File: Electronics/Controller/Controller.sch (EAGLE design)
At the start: 20 parts, among them Q1 IRFD9014, U1 GY-521MPU6050, X1 Battery, X2 Switch

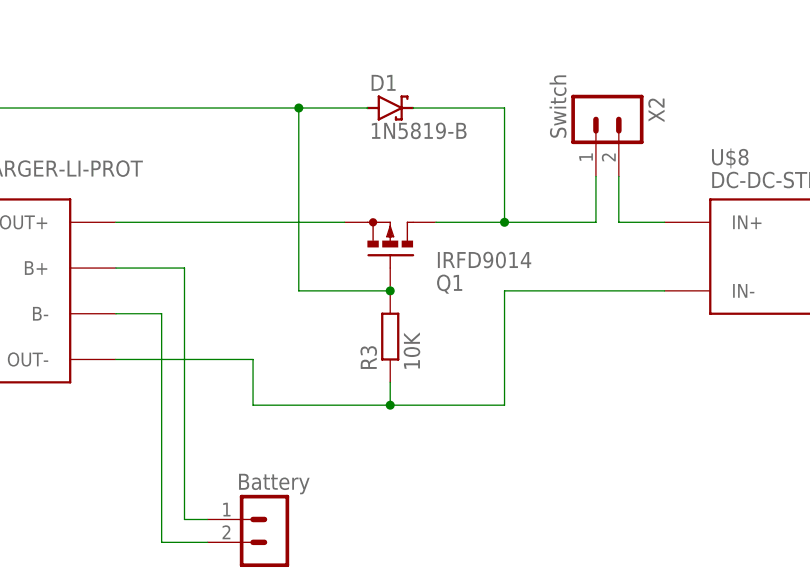
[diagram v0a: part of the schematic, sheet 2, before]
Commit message: Completed all routes
Completed all routes and changed the P-Channel mosfet to a NDP6020P
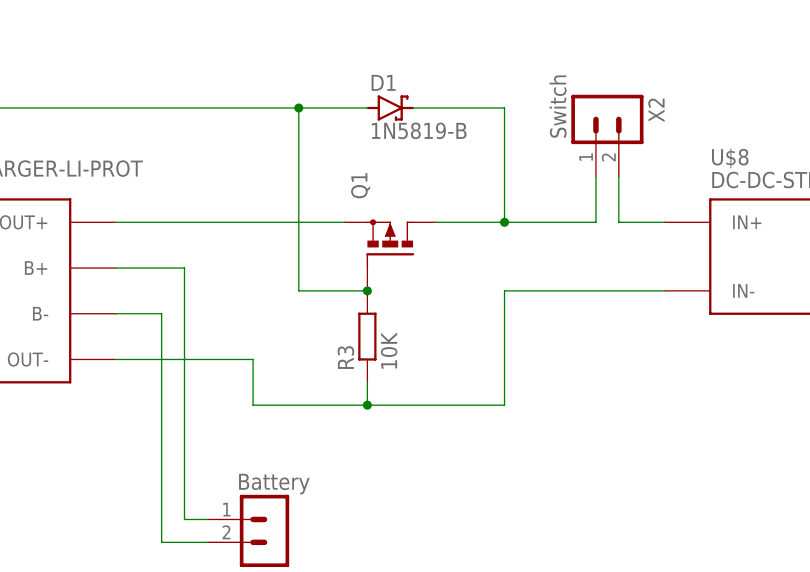
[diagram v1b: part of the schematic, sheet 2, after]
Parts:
- Q1: value IRFD9014 -> (none); device transistor-small-signal:IRFD9120 -> transistor-power:PMOSFET_PTO220BH
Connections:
- new net SW2: R1.2, RIGHT_STICK.SEL-, U$1.12/MISO
- net SW1: no longer R1.2, RIGHT_STICK.SEL-, U$1.12/MISO
- net X-AXIS1: now also U$1.15/A1/T; no longer U$1.14/A0
- net Y-AXIS1: now also U$1.14/A0; no longer U$1.15/A1/T
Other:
- moved on the sheet: R3
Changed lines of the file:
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@@
 <part name="P+4" library="supply1" library_urn="urn:adsk.eagle:library:371" deviceset="+5V" device="" value="+5V_Source"/>
 <part name="GND5" library="supply1" library_urn="urn:adsk.eagle:library:371" deviceset="GND" device="" value="GND_Source"/>
-<part name="Q1" library="transistor-small-signal" library_urn="urn:adsk.eagle:library:401" deviceset="IRFD9120" device="" package3d_urn="urn:adsk.eagle:package:29750/1" value="IRFD9014"/>
 <part name="R3" library="rcl" library_urn="urn:adsk.eagle:library:334" deviceset="R-EU_" device="0207/10" package3d_urn="urn:adsk.eagle:package:23491/2" value="10K"/>
 <part name="D1" library="diode" library_urn="urn:adsk.eagle:library:210" deviceset="1N581*" device="" package3d_urn="urn:adsk.eagle:package:43421/1" technology="9-B"/>
@@
 <part name="P+5" library="supply1" library_urn="urn:adsk.eagle:library:371" deviceset="+5V" device=""/>
 <part name="GND8" library="supply1" library_urn="urn:adsk.eagle:library:371" deviceset="GND" device=""/>
+<part name="Q1" library="transistor-power" library_urn="urn:adsk.eagle:library:400" deviceset="PMOSFET_P" device="TO220BH" package3d_urn="urn:adsk.eagle:package:29490/1"/>
 </parts>
 <sheets>
@@
 </segment>
 <segment>
+<wire x1="43.18" y1="180.34" x2="35.56" y2="180.34" width="0.1524" layer="91"/>
+<label x="35.56" y="180.34" size="1.016" layer="95" rot="R180" xref="yes"/>
+<pinref part="U$1" gate="G$1" pin="15/A1/T"/>
+</segment>
+</net>
+<net name="Y-AXIS1" class="0">
+<segment>
+<pinref part="LEFT_STICK" gate="G$1" pin="H"/>
+<wire x1="335.28" y1="220.98" x2="314.96" y2="220.98" width="0.1524" layer="91"/>
+<label x="314.96" y="220.98" size="1.016" layer="95" rot="R180" xref="yes"/>
+</segment>
+<segment>
 <wire x1="43.18" y1="182.88" x2="35.56" y2="182.88" width="0.1524" layer="91"/>
 <label x="35.56" y="182.88" size="1.016" layer="95" rot="R180" xref="yes"/>
 <pinref part="U$1" gate="G$1" pin="14/A0"/>
-</segment>
-</net>
-<net name="Y-AXIS1" class="0">
-<segment>
-<pinref part="LEFT_STICK" gate="G$1" pin="H"/>
-<wire x1="335.28" y1="220.98" x2="314.96" y2="220.98" width="0.1524" layer="91"/>
-<label x="314.96" y="220.98" size="1.016" layer="95" rot="R180" xref="yes"/>
-</segment>
-<segment>
-<wire x1="43.18" y1="180.34" x2="35.56" y2="180.34" width="0.1524" layer="91"/>
-<label x="35.56" y="180.34" size="1.016" layer="95" rot="R180" xref="yes"/>
-<pinref part="U$1" gate="G$1" pin="15/A1/T"/>
 </segment>
 </net>
@@
 </segment>
 <segment>
-<label x="314.96" y="172.72" size="1.016" layer="95" rot="R180" xref="yes"/>
-<pinref part="RIGHT_STICK" gate="G$1" pin="SEL-"/>
-<pinref part="R1" gate="G$1" pin="2"/>
-<wire x1="335.28" y1="172.72" x2="330.2" y2="172.72" width="0.1524" layer="91"/>
-<wire x1="330.2" y1="172.72" x2="314.96" y2="172.72" width="0.1524" layer="91"/>
-<junction x="330.2" y="172.72"/>
-</segment>
-<segment>
 <label x="35.56" y="190.5" size="1.016" layer="95" rot="R180" xref="yes"/>
 <wire x1="43.18" y1="190.5" x2="35.56" y2="190.5" width="0.1524" layer="91"/>
 <pinref part="U$1" gate="G$1" pin="11/MOSI"/>
-</segment>
-<segment>
-<label x="35.56" y="187.96" size="1.016" layer="95" rot="R180" xref="yes"/>
-<wire x1="43.18" y1="187.96" x2="35.56" y2="187.96" width="0.1524" layer="91"/>
-<pinref part="U$1" gate="G$1" pin="12/MISO"/>
 </segment>
 </net>
@@
 </segment>
 </net>
+<net name="SW2" class="0">
+<segment>
+<label x="35.56" y="187.96" size="1.016" layer="95" rot="R180" xref="yes"/>
+<wire x1="43.18" y1="187.96" x2="35.56" y2="187.96" width="0.1524" layer="91"/>
+<pinref part="U$1" gate="G$1" pin="12/MISO"/>
+</segment>
+<segment>
+<label x="314.96" y="172.72" size="1.016" layer="95" rot="R180" xref="yes"/>
+<pinref part="RIGHT_STICK" gate="G$1" pin="SEL-"/>
+<pinref part="R1" gate="G$1" pin="2"/>
+<wire x1="335.28" y1="172.72" x2="330.2" y2="172.72" width="0.1524" layer="91"/>
+<wire x1="330.2" y1="172.72" x2="314.96" y2="172.72" width="0.1524" layer="91"/>
+<junction x="330.2" y="172.72"/>
+</segment>
+</net>
 </nets>
 </sheet>
@@
 <attribute name="VALUE" x="48.26" y="86.36" size="1.778" layer="96"/>
 </instance>
-<instance part="Q1" gate="A" x="116.84" y="106.68" smashed="yes" rot="R90">
-<attribute name="NAME" x="121.92" y="101.6" size="1.778" layer="95"/>
-<attribute name="VALUE" x="121.92" y="104.14" size="1.778" layer="96"/>
-</instance>
-<instance part="R3" gate="G$1" x="116.84" y="96.52" smashed="yes" rot="R90">
-<attribute name="NAME" x="115.3414" y="92.71" size="1.778" layer="95" rot="R90"/>
-<attribute name="VALUE" x="120.142" y="92.71" size="1.778" layer="96" rot="R90"/>
+<instance part="R3" gate="G$1" x="114.3" y="96.52" smashed="yes" rot="R90">
+<attribute name="NAME" x="112.8014" y="92.71" size="1.778" layer="95" rot="R90"/>
+<attribute name="VALUE" x="117.602" y="92.71" size="1.778" layer="96" rot="R90"/>
 </instance>
 <instance part="D1" gate="G$1" x="116.84" y="121.92" smashed="yes">
@@
 <attribute name="VALUE" x="134.62" y="125.73" size="1.778" layer="96" rot="R270"/>
 <attribute name="NAME" x="145.542" y="123.19" size="1.778" layer="95" rot="R270"/>
+</instance>
+<instance part="Q1" gate="G$1" x="116.84" y="106.68" smashed="yes" rot="R90">
+<attribute name="NAME" x="114.3" y="111.76" size="1.778" layer="95" rot="R90"/>
+<attribute name="VALUE" x="116.84" y="111.76" size="1.778" layer="96" rot="R90"/>
 </instance>
 </instances>
@@
 <pinref part="U$5" gate="G$1" pin="OUT+"/>
 <wire x1="86.36" y1="109.22" x2="111.76" y2="109.22" width="0.1524" layer="91"/>
-<pinref part="Q1" gate="A" pin="S"/>
+<pinref part="Q1" gate="G$1" pin="S"/>
 </segment>
 </net>
@@
 <wire x1="50.8" y1="121.92" x2="50.8" y2="124.46" width="0.1524" layer="91"/>
 <junction x="50.8" y="121.92"/>
-<pinref part="Q1" gate="A" pin="G"/>
 <pinref part="R3" gate="G$1" pin="2"/>
-<wire x1="116.84" y1="101.6" x2="106.68" y2="101.6" width="0.1524" layer="91"/>
-<junction x="116.84" y="101.6"/>
+<wire x1="114.3" y1="101.6" x2="106.68" y2="101.6" width="0.1524" layer="91"/>
 <wire x1="106.68" y1="101.6" x2="106.68" y2="121.92" width="0.1524" layer="91"/>
 <junction x="106.68" y="121.92"/>
+<pinref part="Q1" gate="G$1" pin="G"/>
+<junction x="114.3" y="101.6"/>
 </segment>
 <segment>
@@
 <segment>
 <pinref part="R3" gate="G$1" pin="1"/>
-<wire x1="116.84" y1="88.9" x2="116.84" y2="91.44" width="0.1524" layer="91"/>
-<wire x1="101.6" y1="88.9" x2="116.84" y2="88.9" width="0.1524" layer="91"/>
+<wire x1="114.3" y1="88.9" x2="114.3" y2="91.44" width="0.1524" layer="91"/>
+<wire x1="101.6" y1="88.9" x2="114.3" y2="88.9" width="0.1524" layer="91"/>
 <pinref part="U$5" gate="G$1" pin="OUT-"/>
 <wire x1="86.36" y1="93.98" x2="101.6" y2="93.98" width="0.1524" layer="91"/>
@@
 <pinref part="U$8" gate="G$1" pin="IN-"/>
 <wire x1="147.32" y1="101.6" x2="129.54" y2="101.6" width="0.1524" layer="91"/>
-<wire x1="116.84" y1="88.9" x2="129.54" y2="88.9" width="0.1524" layer="91"/>
-<junction x="116.84" y="88.9"/>
+<wire x1="114.3" y1="88.9" x2="129.54" y2="88.9" width="0.1524" layer="91"/>
+<junction x="114.3" y="88.9"/>
 </segment>
 </net>
 <net name="N$4" class="0">
 <segment>
-<pinref part="Q1" gate="A" pin="D"/>
 <wire x1="121.92" y1="109.22" x2="129.54" y2="109.22" width="0.1524" layer="91"/>
 <pinref part="D1" gate="G$1" pin="C"/>
@@
 <wire x1="139.7" y1="109.22" x2="139.7" y2="114.3" width="0.1524" layer="91"/>
 <junction x="129.54" y="109.22"/>
-</segment>
-</net>
+<pinref part="Q1" gate="G$1" pin="D"/>
+</segment>
+</net>

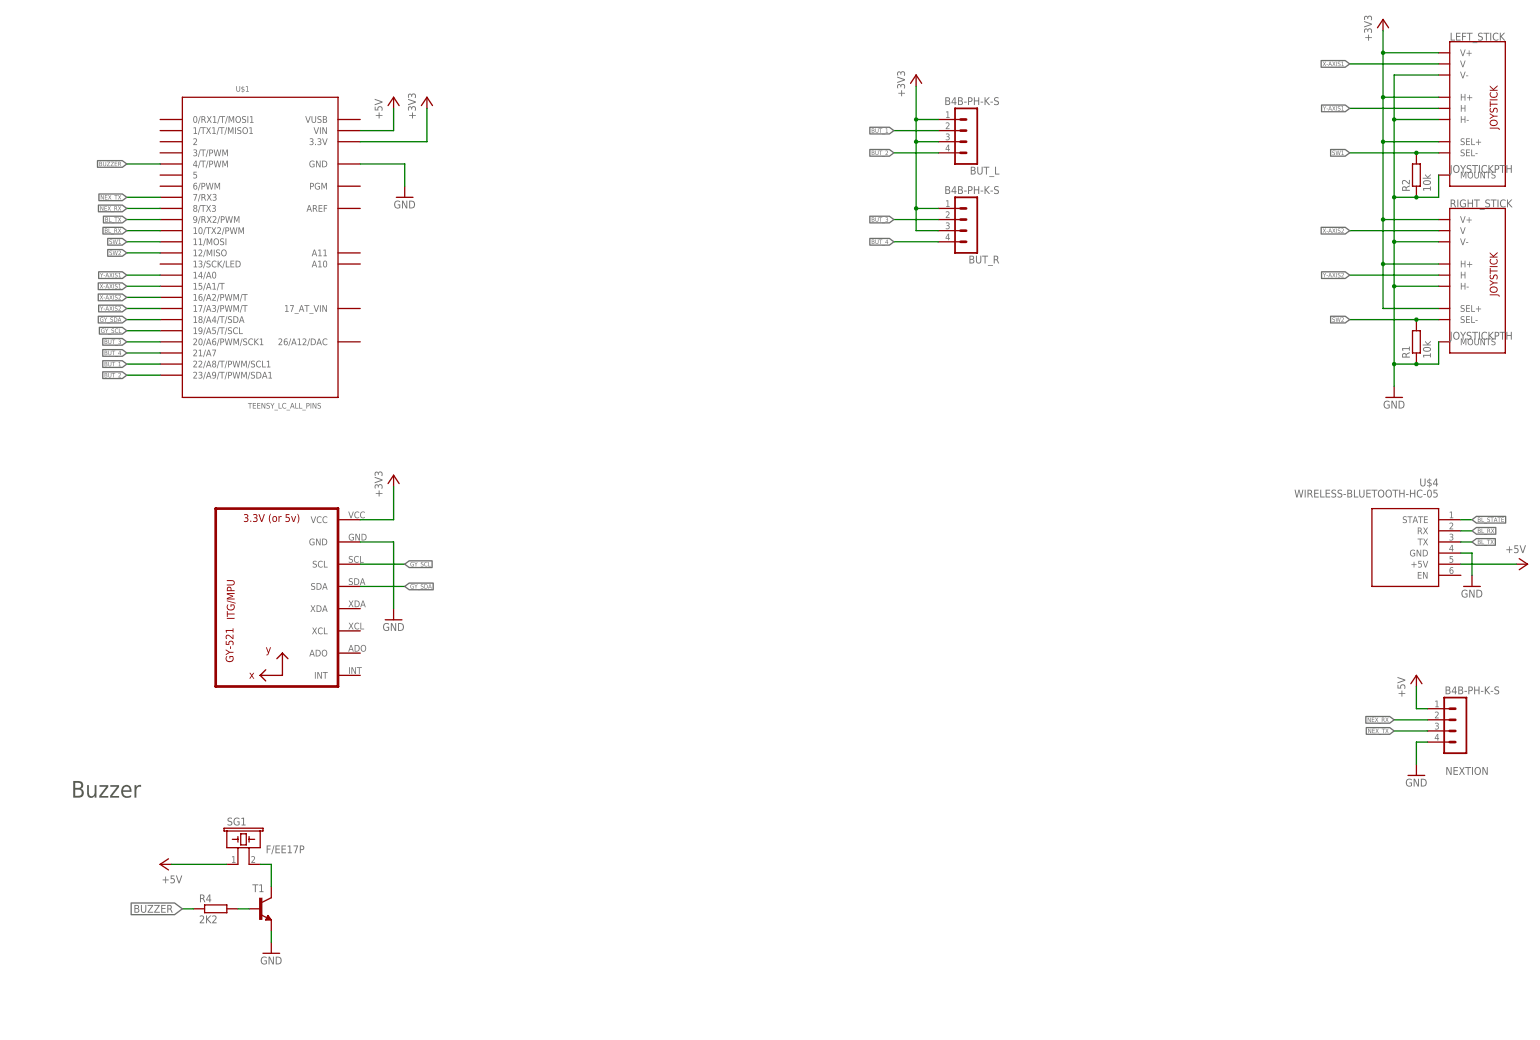
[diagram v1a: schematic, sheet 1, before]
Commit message: Added Nextion in Board Layout
Added nextion in board layout and made the height 10mm for a standoff. Changed de JST connectors from 2mm to 2,54 spacing
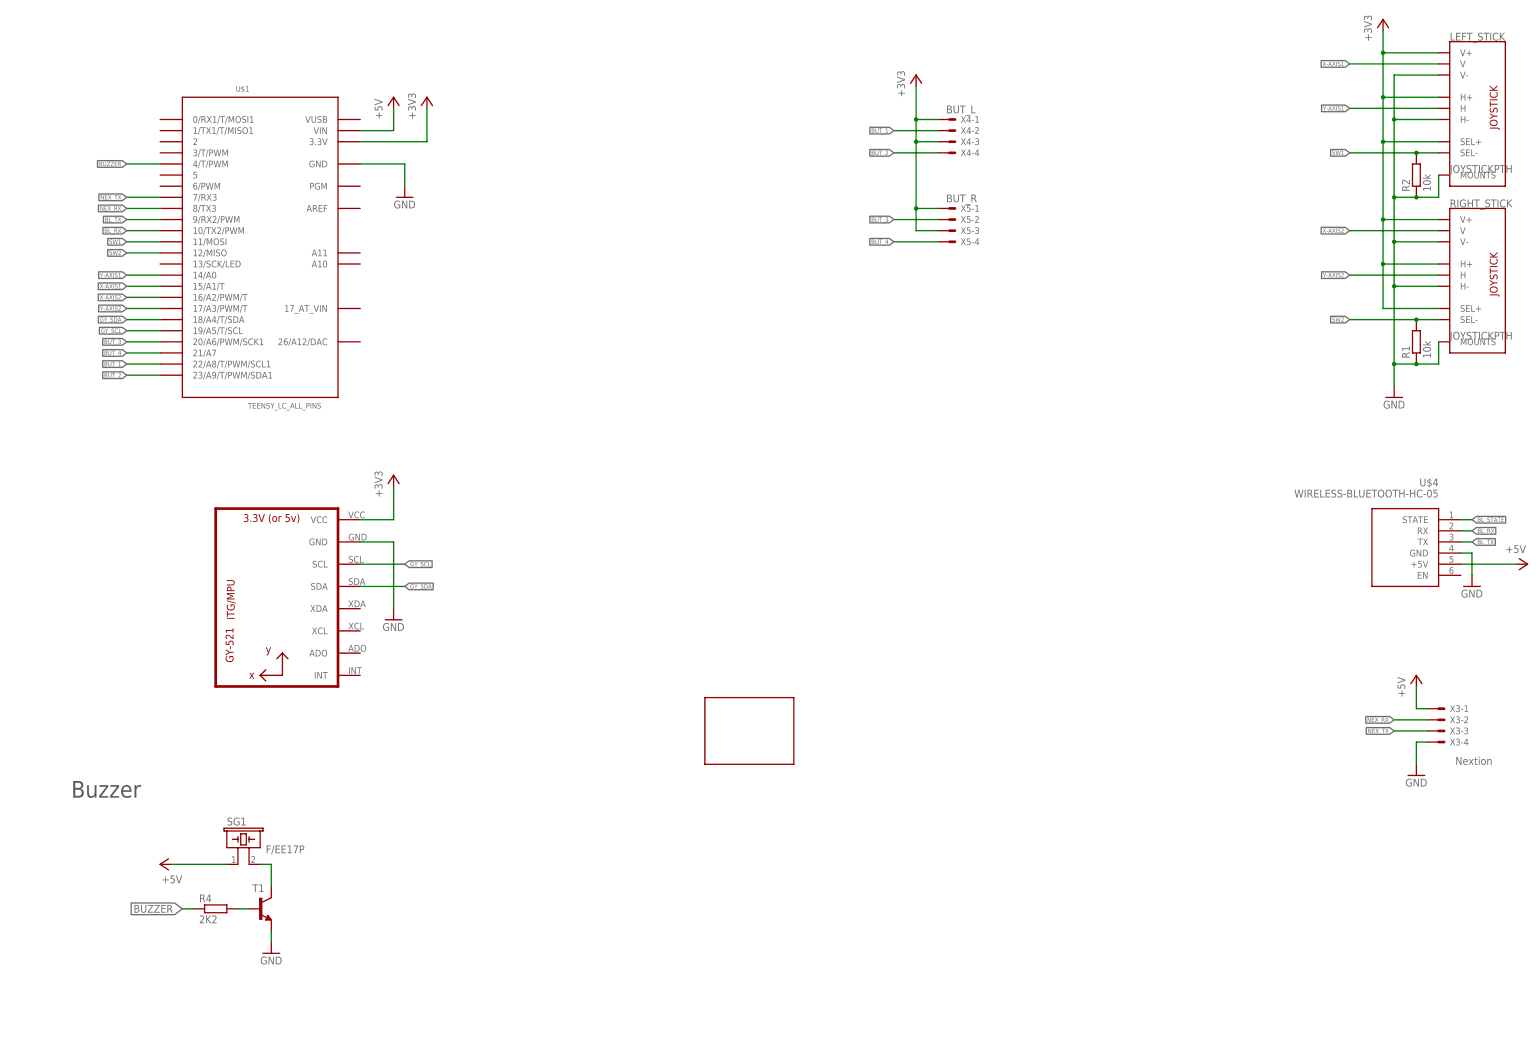
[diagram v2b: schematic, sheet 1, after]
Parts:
- removed BUT_L, BUT_R, NEXTION: B4B-PH-K-S, con-JST PH:B4B-PH-K-S
- added U$9: NX4832K035, Nextion:NX4832K035
- added X3: Nextion, Rembrandt Electronics - JST XH Connectors v1-0:JST-XH-04-PIN-LONG-PAD
- added X4: BUT_L, Rembrandt Electronics - JST XH Connectors v1-0:JST-XH-04-PIN-LONG-PAD
- added X5: BUT_R, Rembrandt Electronics - JST XH Connectors v1-0:JST-XH-04-PIN-LONG-PAD
- X1, X2: device con-JST PH:B2B-PH-K-S -> Rembrandt Electronics - JST XH Connectors v1-0:JST-XH-02-PIN-LONG-PAD
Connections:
- new net N$9: D1.A, Q1.G, R3.2, U$5.IN+
- net +3V3: now also X4-1.S, X4-3.S, X5-1.S, X5-3.S; no longer BUT_L.1, BUT_L.3, BUT_R.1, BUT_R.3
- net +5V: now also X3-1.S; no longer D1.A, NEXTION.1, Q1.G, R3.2, U$5.IN+
- net BUT_1: now also X4-2.S; no longer BUT_L.2
- net BUT_2: now also X4-4.S; no longer BUT_L.4
- net BUT_3: now also X5-2.S; no longer BUT_R.2
- net BUT_4: now also X5-4.S; no longer BUT_R.4
- net GND: now also X3-4.S; no longer NEXTION.4, U$5.IN-
- net N$2: now also X1-1.S; no longer X1.1
- net N$3: now also X1-2.S; no longer X1.2
- net N$4: now also X2-1.S; no longer X2.1
- net N$6: now also X2-2.S; no longer X2.2
- net NEX_RX: now also X3-2.S; no longer NEXTION.2
- net NEX_TX: now also X3-3.S; no longer NEXTION.3

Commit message: Frame change
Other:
- note removed: "Buzzer"
- moved on the sheet: LEFT_STICK, R1, R2, R4, RIGHT_STICK, SG1, T1, U$1, U$4, X3-1, X3-2, X3-3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
